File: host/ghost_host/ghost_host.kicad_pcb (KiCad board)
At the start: 2 copper layers, 127.5 x 68.5 mm, 115 parts, among them J1 RGB_3_Pin_Connector, J10 Conn_01x06, J11 Conn_01x04, J12 RJ12_Shielded, J13 Conn_01x06, J14 Conn_01x04, J15 RJ12_Shielded, J16 Conn_01x06, J17 Conn_01x04, J18 RJ12_Shielded, J19 Conn_01x06, J2 Conn_01x04, J20 Conn_01x04, J21 RJ12_Shielded, J22 Conn_01x06, J23 RJ12_Shielded, J24 Conn_01x06, J25 Conn_01x06, J3 Conn_01x04, J4 RJ12_Shielded, J5 Conn_01x04, J6 RJ12_Shielded, J7 Conn_01x06, J8 Conn_01x04, J9 RJ12_Shielded, U1 PCA9615DP, U2 PCA9615DP, U3 PCA9615DP, U4 PCA9615DP, U5 PCA9615DP, U6 PCA9615DP, U7 PCA9615DP, U8 PCA9615DP, U9 ProMicro

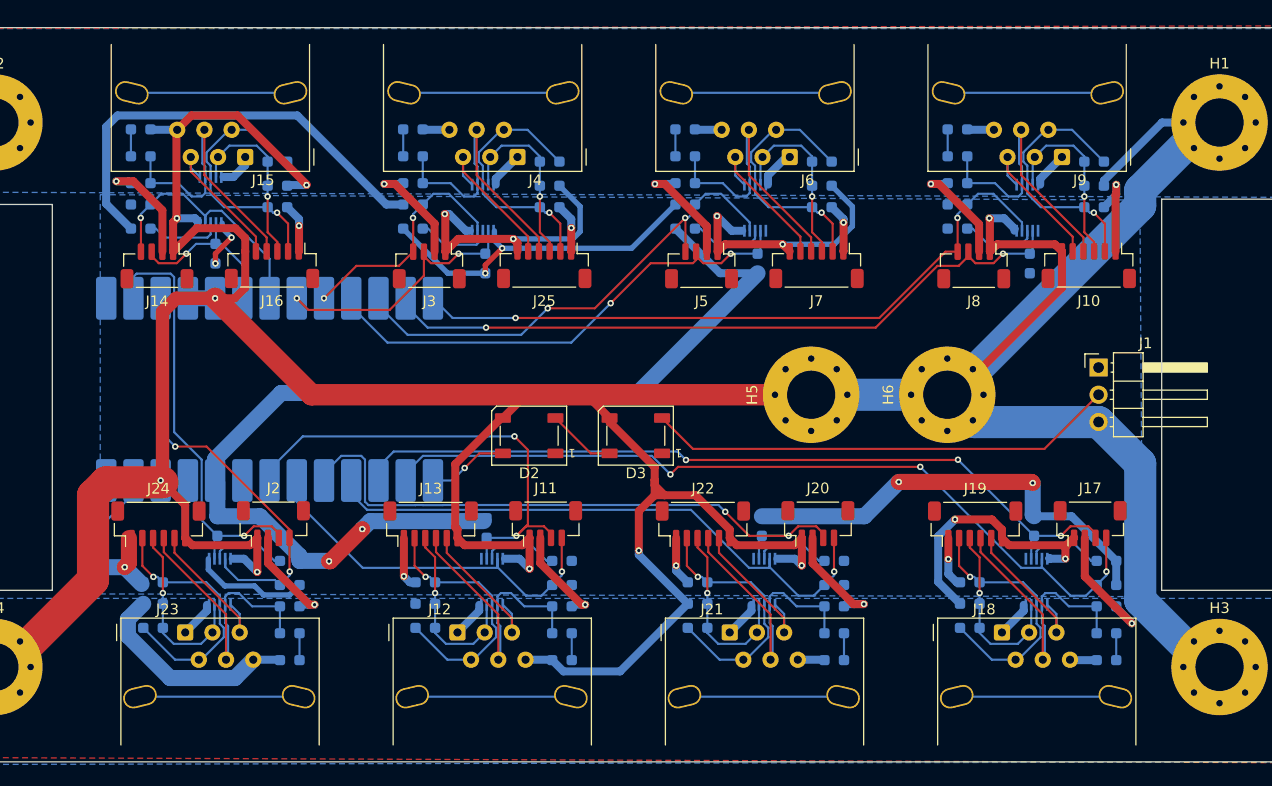
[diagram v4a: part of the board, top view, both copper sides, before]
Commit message: labels added to Host board
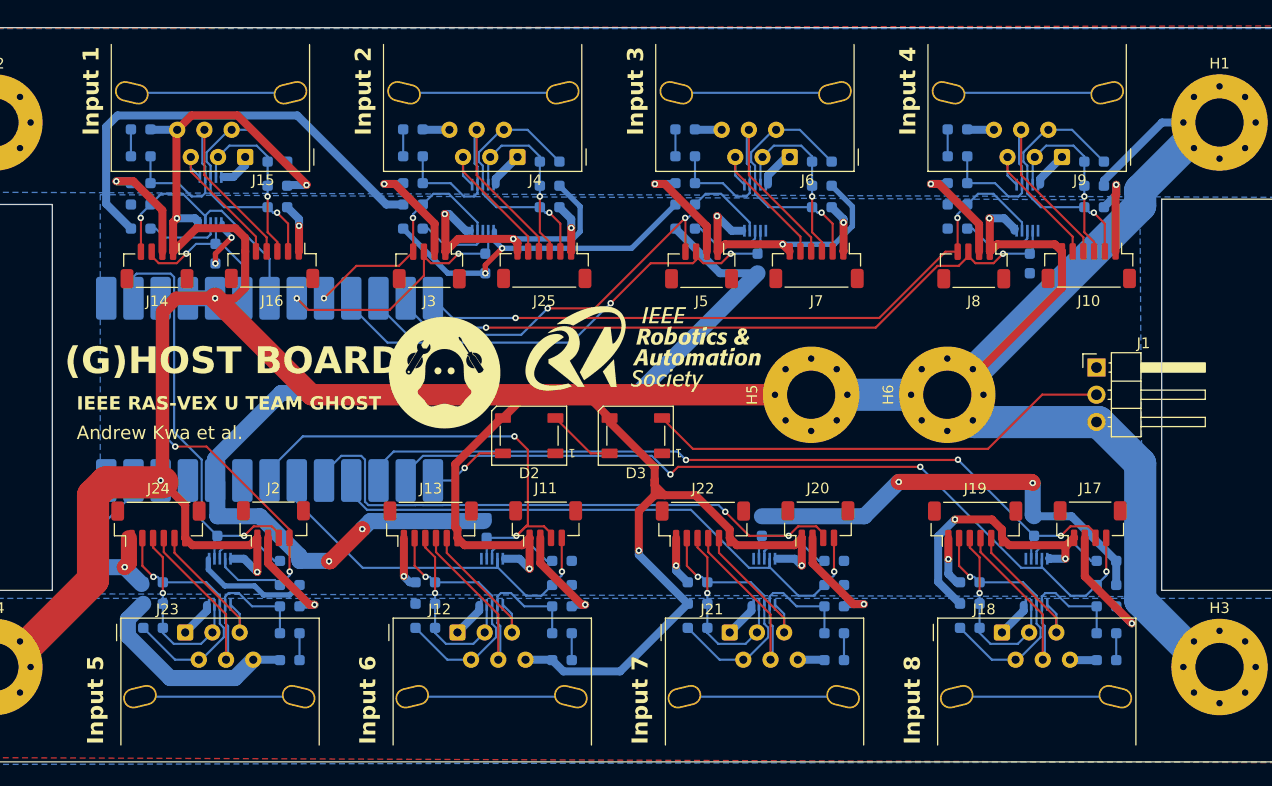
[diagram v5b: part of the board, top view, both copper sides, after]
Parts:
- added G***: LOGO, LOGO, F.Cu at (128.8, 86.1)
- added G***: LOGO, LOGO, F.Cu at (147.4, 83.9)
- moved J1 0.20 mm to (189.7, 85.6)
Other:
- board text added: "(G)HOST BOARD"
- board text added: "Andrew Kwa et al."
- board text added: "IEEE RAS-VEX U TEAM GHOST"
- board text added: "INPUT 1 - GPIO 2/3 INPUT 2 - GPIO 4/5 INPUT 3 - GPIO 6/7 INPUT 4 - GPIO 8/9 INPUT 5 - GPIO 0/1 INPUT 6 - GPIO 28/27 INPUT 7 - GPIO 26/18 INPUT 8 - GPIO 20/19"
- board text added: "Input 1"
- board text added: "Input 2"
- board text added: "Input 3"
- board text added: "Input 4"
- board text added: "Input 5"
- board text added: "Input 6"
- board text added: "Input 7"
- board text added: "Input 8"
- board text added: "PINOUT - SDA/SCL"
- board text removed: "plz double check that the holes r half inch spacing"

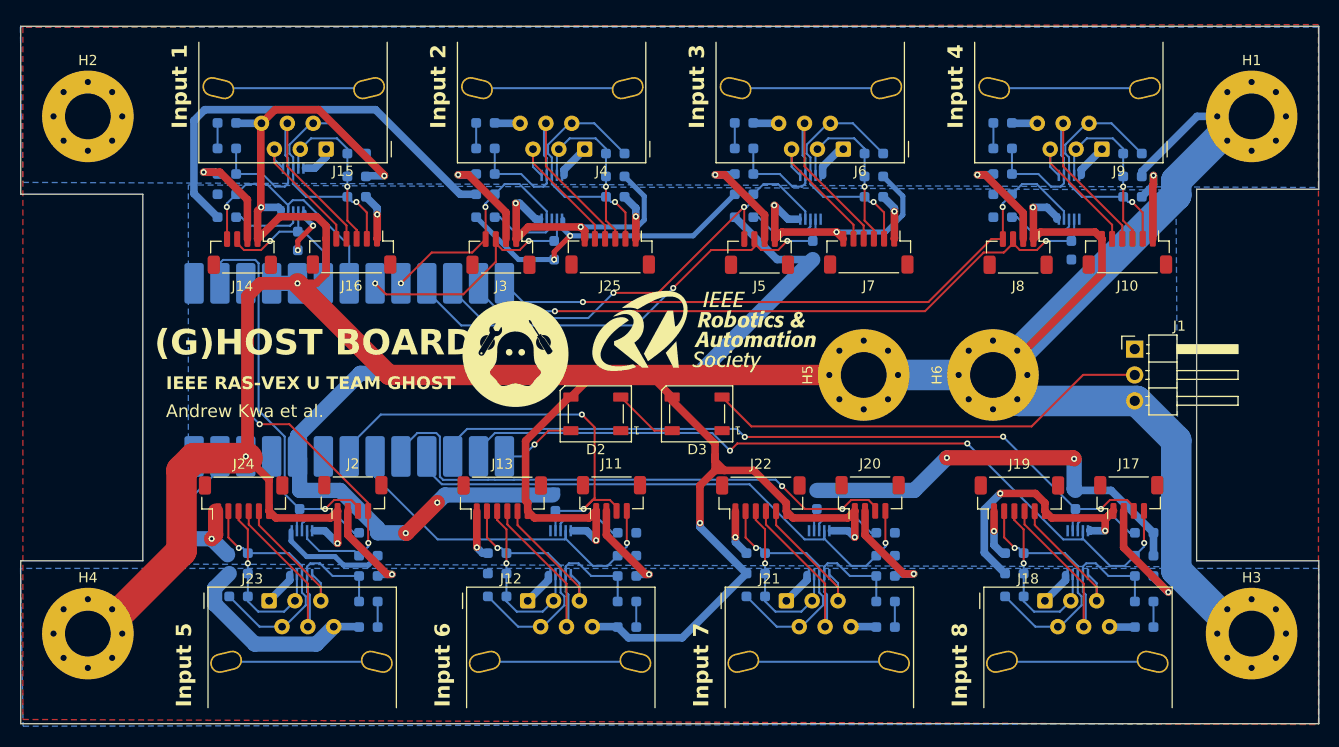
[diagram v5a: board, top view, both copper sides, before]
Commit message: pcb review, added 3d models
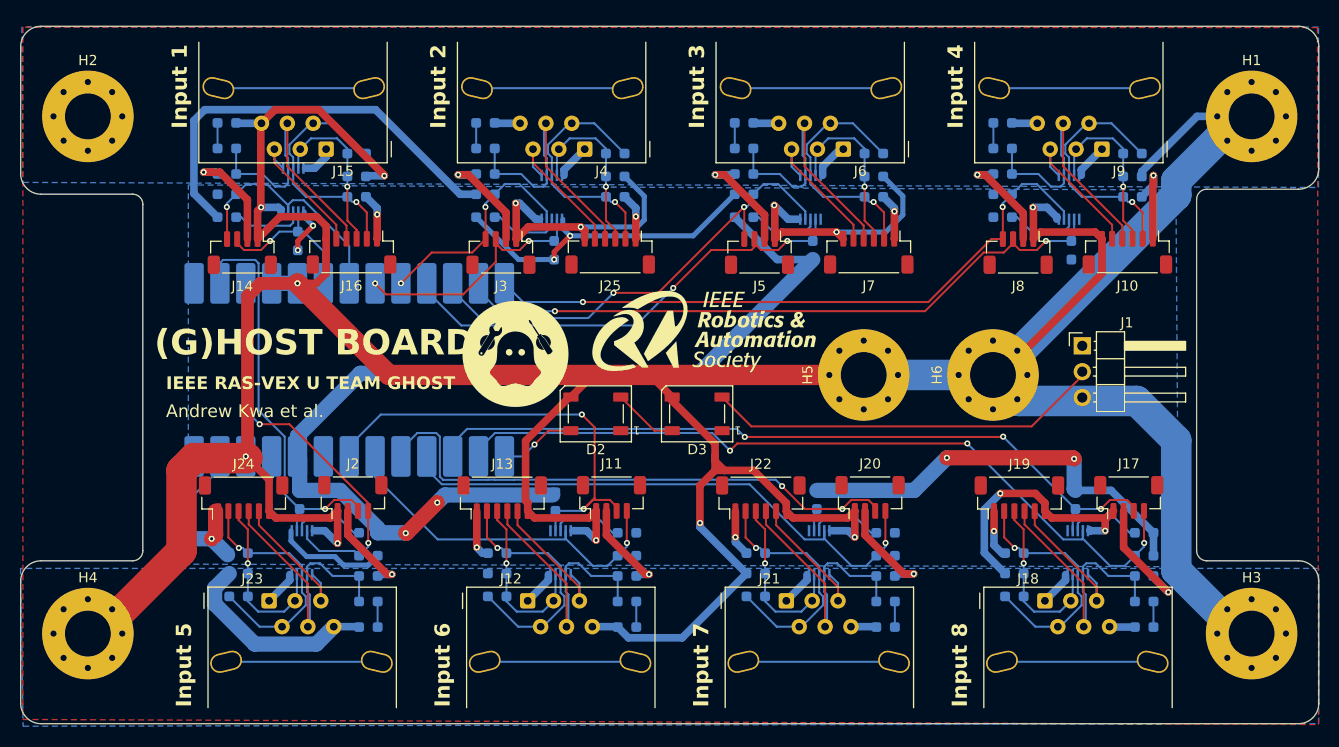
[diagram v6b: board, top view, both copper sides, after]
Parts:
- U9: value ProMicro -> kb2040
- moved J1 5.16 mm to (184.6, 85.3)
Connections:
- J2 pad 3: /sda1 -> /sda5
- J2 pad 4: /scl1 -> /scl5
- J8 pad 3: /sda5 -> /sda1
- J8 pad 4: /scl5 -> /scl1
- R1 pad 2: /sda1 -> /sda5
- R10 pad 2: /scl5 -> /scl1
- R2 pad 2: /scl1 -> /scl5
- R8 pad 2: /sda5 -> /sda1
- U1 pad 2: /sda1 -> /sda5
- U1 pad 4: /scl1 -> /scl5
- U4 pad 2: /sda5 -> /sda1
- U4 pad 4: /scl5 -> /scl1
- U9 pad 12: /sda5 -> /sda1
- U9 pad 13: /scl5 -> /scl1
- U9 pad 2: /sda1 -> /sda5
- U9 pad 3: /scl1 -> /scl5
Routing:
- net /sda5: track 66.3 -> 40.9 mm, vias 2 -> 1
- net /sda1: track 40.9 -> 66.3 mm, vias 1 -> 2
- net /scl5: track 64.5 -> 41.2 mm
- net /scl1: track 41.2 -> 64.5 mm
- net Net-(D3-DOUT): track 43.8 -> 39.1 mm
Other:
- outline, holes or cut-outs redrawn
- board text added: "INPUT 1 - GPIO 8/9 INPUT 2 - GPIO 2/3 INPUT 3 - GPIO 4/5 INPUT 4 - GPIO 6/7 INPUT 5 - GPIO 0/1 INPUT 6 - GPIO 28/27 INPUT 7 - GPIO 26/18 INPUT 8 - GPIO 20/19"
- board text removed: "INPUT 1 - GPIO 2/3 INPUT 2 - GPIO 4/5 INPUT 3 - GPIO 6/7 INPUT 4 - GPIO 8/9 INPUT 5 - GPIO 0/1 INPUT 6 - GPIO 28/27 INPUT 7 - GPIO 26/18 INPUT 8 - GPIO 20/19"

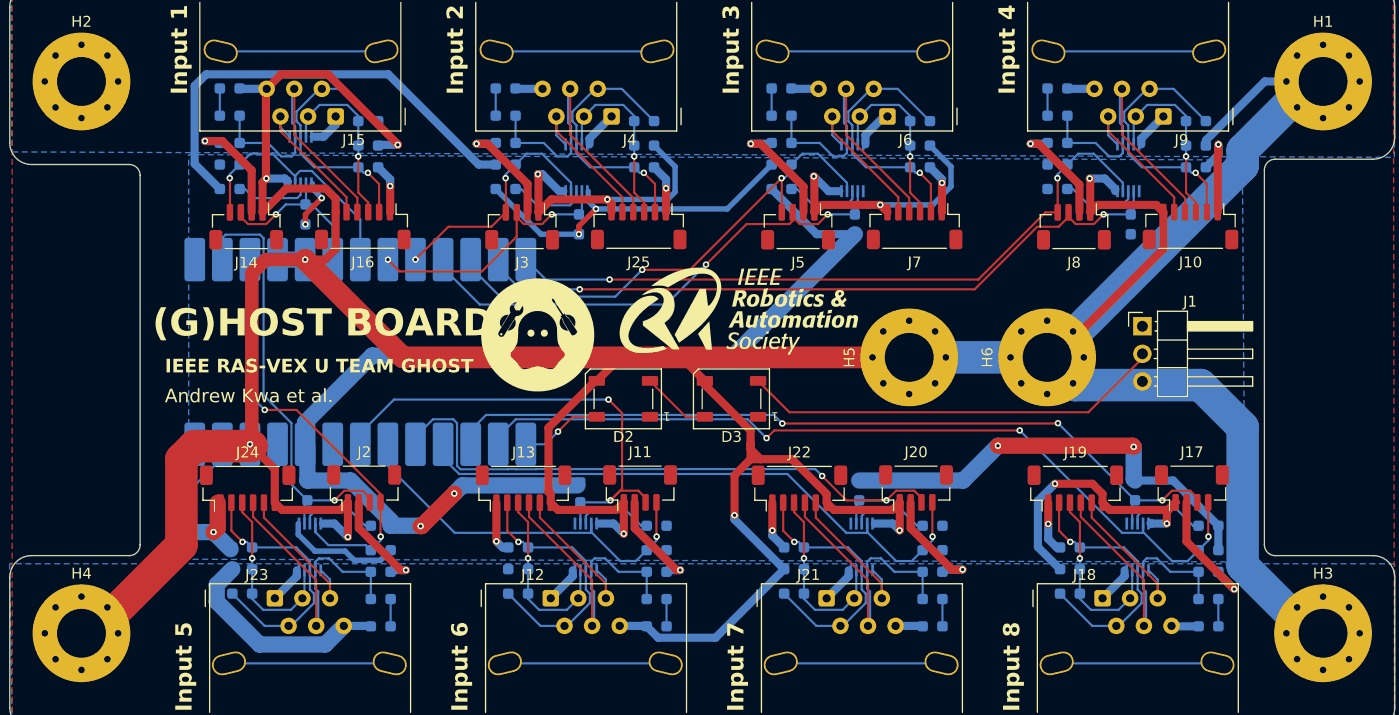
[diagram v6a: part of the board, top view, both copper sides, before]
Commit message: rearranged some parts
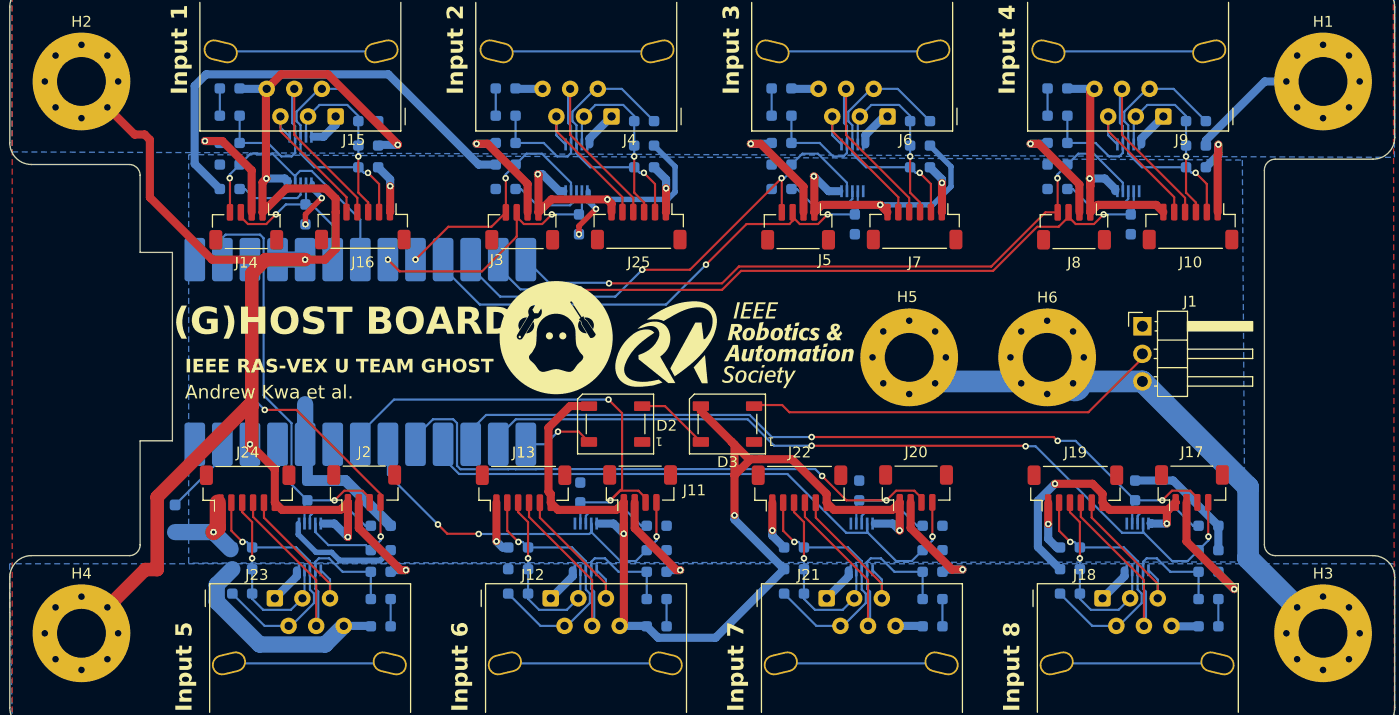
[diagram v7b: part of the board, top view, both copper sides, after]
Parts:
- J10, J13, J16, J19, J22, J24, J25, J7: footprint Connector_JST:JST_SH_BM06B-SRSS-TB_1x06-1MP_P1.00mm_Vertical -> RJ12_Pin_Connector:JST_SH_BM06B-SRSS-TB_1x06-1MP_P1.00mm_Vertical
- J11, J14, J17, J2, J20, J3, J5, J8: footprint Connector_JST:JST_SH_BM04B-SRSS-TB_1x04-1MP_P1.00mm_Vertical -> RJ12_Pin_Connector:JST_SH_BM04B-SRSS-TB_1x04-1MP_P1.00mm_Vertical
- moved G*** 3.13 mm to (147.0, 87.0)
- moved D2 2.42 mm to (136.1, 94.3)
- moved D3 2.34 mm to (146.3, 94.3)
- moved G*** 1.72 mm to (130.6, 86.3)
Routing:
- net +3.3V: track 232.3 -> 90.7 mm, vias 8 -> 4
- net GND: track 537.0 -> 461.4 mm
- net /scl6: track 36.3 -> 37.6 mm, vias 1 -> 3
- net /Neopixel_Data: track 7.58 -> 6.69 mm
- net /scl8: track 78.6 -> 78.0 mm
- net Net-(D3-DOUT): track 39.1 -> 38.6 mm
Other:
- outline, holes or cut-outs redrawn

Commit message: more formatting
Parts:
- moved G*** 1.10 mm to (147.1, 85.9)
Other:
- outline, holes or cut-outs redrawn
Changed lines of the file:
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@@
 	(footprint "LOGO"
 		(layer "F.Cu")
-		(at 147 87)
+		(at 147.1 85.9)
 		(property "Reference" "G***"
 			(at 0 0 0)
@@
 	(gr_line
 		(start 82.28 106.415)
-		(end 91.28 106.415)
+		(end 91.3 106.415)
 		(stroke
 			(width 0.05)
@@
 		(layer "Edge.Cuts")
 	)
+	(gr_line
+		(start 205.78 69.92)
+		(end 196.78 69.92)
+		(stroke
+			(width 0.05)
+			(type solid)
+		)
+		(layer "Edge.Cuts")
+	)
 	(gr_arc
-		(start 92.28 105.415)
-		(mid 91.987107 106.122107)
-		(end 91.28 106.415)
+		(start 95.25 95.9)
+		(mid 94.957107 96.607107)
+		(end 94.25 96.9)
 		(stroke
 			(width 0.05)
@@
 	)
 	(gr_line
-		(start 205.78 69.92)
-		(end 196.78 69.92)
+		(start 93.28 78.9)
+		(end 94.25 78.9)
 		(stroke
 			(width 0.05)
-			(type solid)
+			(type default)
 		)
 		(layer "Edge.Cuts")
 	)
 	(gr_line
-		(start 92.28 78.5)
-		(end 92.28 71.41)
+		(start 92.28 77.9)
+		(end 92.28 71.4)
+		(stroke
+			(width 0.05)
+			(type solid)
+		)
+		(layer "Edge.Cuts")
+	)
+	(gr_arc
+		(start 93.28 78.9)
+		(mid 92.572893 78.607107)
+		(end 92.28 77.9)
 		(stroke
 			(width 0.05)
@@
 	)
 	(gr_line
-		(start 95.25 78.5)
-		(end 95.25 95.85)
+		(start 95.25 79.9)
+		(end 95.25 95.9)
+		(stroke
+			(width 0.05)
+			(type default)
+		)
+		(layer "Edge.Cuts")
+	)
+	(gr_arc
+		(start 92.3 105.415)
+		(mid 92.007107 106.122107)
+		(end 91.3 106.415)
 		(stroke
 			(width 0.05)
@@
 		(layer "Edge.Cuts")
 	)
-	(gr_line
-		(start 92.28 95.85)
-		(end 92.28 105.415)
+	(gr_arc
+		(start 92.3 97.9)
+		(mid 92.592893 97.192893)
+		(end 93.3 96.9)
 		(stroke
 			(width 0.05)
@@
 		(layer "Edge.Cuts")
 	)
+	(gr_arc
+		(start 94.25 78.9)
+		(mid 94.957107 79.192893)
+		(end 95.25 79.9)
+		(stroke
+			(width 0.05)
+			(type default)
+		)
+		(layer "Edge.Cuts")
+	)
+	(gr_line
+		(start 92.3 105.415)
+		(end 92.3 97.9)
+		(stroke
+			(width 0.05)
+			(type solid)
+		)
+		(layer "Edge.Cuts")
+	)
 	(gr_line
 		(start 91.28 70.41)
@@
 		(layer "Edge.Cuts")
 	)
-	(gr_line
-		(start 95.25 95.85)
-		(end 92.28 95.85)
+	(gr_arc
+		(start 207.78 67.92)
+		(mid 207.194214 69.334214)
+		(end 205.78 69.92)
 		(stroke
 			(width 0.05)
@@
 		(layer "Edge.Cuts")
 	)
-	(gr_arc
-		(start 207.78 67.92)
-		(mid 207.194214 69.334214)
-		(end 205.78 69.92)
+	(gr_line
+		(start 93.3 96.9)
+		(end 94.25 96.9)
 		(stroke
 			(width 0.05)
@@
 		(stroke
 			(width 0.05)
-			(type default)
-		)
-		(layer "Edge.Cuts")
-	)
-	(gr_line
-		(start 92.28 78.5)
-		(end 95.25 78.5)
-		(stroke
-			(width 0.05)
